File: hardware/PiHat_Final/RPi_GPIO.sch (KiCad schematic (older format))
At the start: 1 part, among them J2 RPi_GPIO

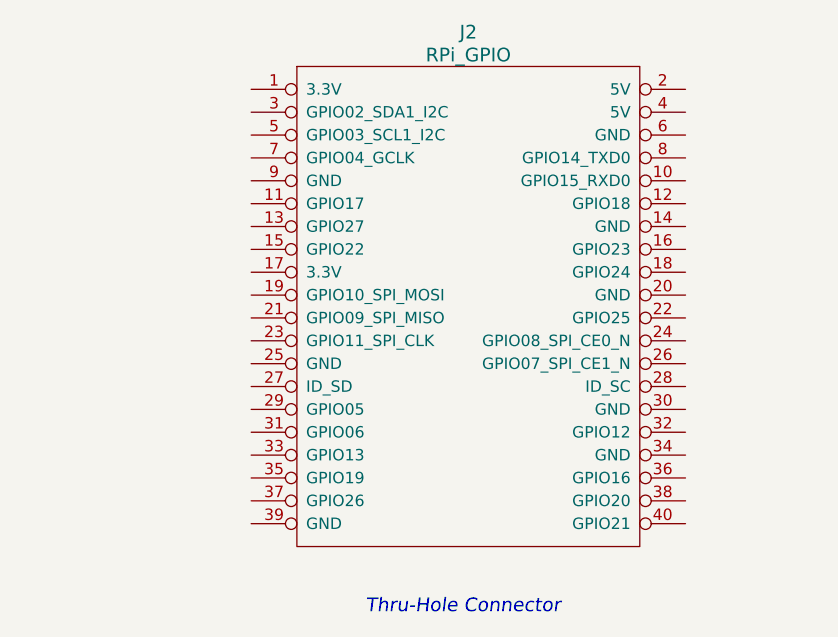
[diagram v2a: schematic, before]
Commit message: Transciever wiring & Power Distribution Changes, modified footprint for Edge SMA, swapped TX/RX on ANTSEL
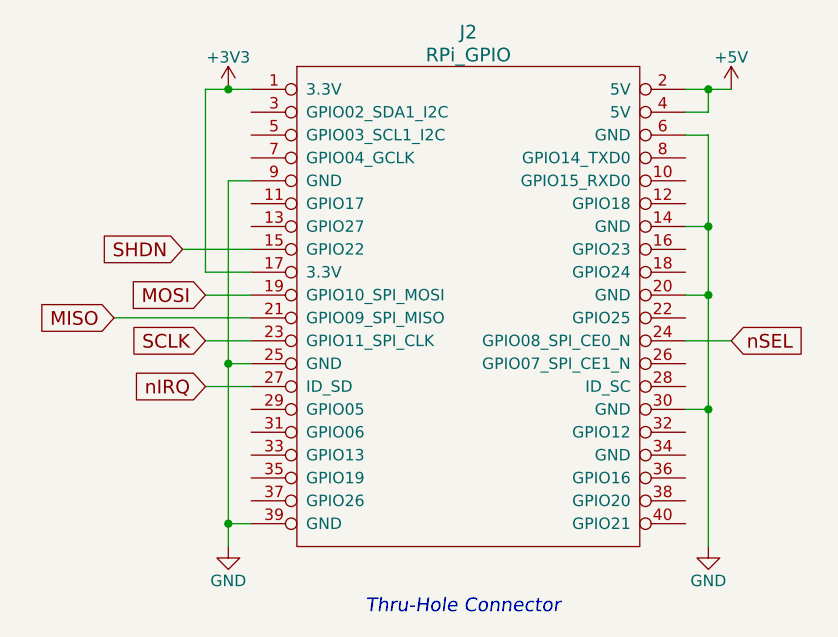
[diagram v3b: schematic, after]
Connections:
- net +3V3: now reaches J2.1 (3.3V)
- net +3V3: now also J2.17 (3.3V)
- net GND: now reaches J2.14 (GND)
- net GND: now also J2.20 (GND), J2.25 (GND), J2.30 (GND), J2.39 (GND), J2.6 (GND), J2.9 (GND)
- net SHDN: now reaches J2.15 (GPIO22)
- net MOSI: now reaches J2.19 (GPIO10_SPI_MOSI)
- net +5V: now reaches J2.2 (5V)
- net +5V: now also J2.4 (5V)
- net MISO: now reaches J2.21 (GPIO09_SPI_MISO)
- net SCLK: now reaches J2.23 (GPIO11_SPI_CLK)
- net nSEL: now reaches J2.24 (GPIO08_SPI_CE0_N)
- net nIRQ: now reaches J2.27 (ID_SD)
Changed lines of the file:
@@
 Text Notes 7800 5000 0    60   Italic 0
 Thru-Hole Connector
+Wire Wire Line
+	9200 2800 9300 2800
+Wire Wire Line
+	9300 2800 9300 2700
+Wire Wire Line
+	9200 2700 9400 2700
+Connection ~ 9300 2700
+Wire Wire Line
+	7100 2700 7300 2700
+$Comp
+L +5V #PWR01
+U 1 1 58FBDD1D
+P 9400 2700
+F 0 "#PWR01" H 9400 2550 50  0001 C CNN
+F 1 "+5V" H 9400 2840 50  0000 C CNN
+F 2 "" H 9400 2700 50  0001 C CNN
+F 3 "" H 9400 2700 50  0001 C CNN
+	1    9400 2700
+	1    0    0    -1
+$EndComp
+$Comp
+L +3V3 #PWR02
+U 1 1 58FBDD33
+P 7200 2700
+F 0 "#PWR02" H 7200 2550 50  0001 C CNN
+F 1 "+3V3" H 7200 2840 50  0000 C CNN
+F 2 "" H 7200 2700 50  0001 C CNN
+F 3 "" H 7200 2700 50  0001 C CNN
+	1    7200 2700
+	1    0    0    -1
+$EndComp
+Wire Wire Line
+	7300 3900 7200 3900
+Wire Wire Line
+	7200 3100 7200 4700
+Wire Wire Line
+	7300 4600 7200 4600
+Connection ~ 7200 4600
+$Comp
+L GND #PWR03
+U 1 1 58FBDD61
+P 7200 4700
+F 0 "#PWR03" H 7200 4450 50  0001 C CNN
+F 1 "GND" H 7200 4550 50  0000 C CNN
+F 2 "" H 7200 4700 50  0001 C CNN
+F 3 "" H 7200 4700 50  0001 C CNN
+	1    7200 4700
+	1    0    0    -1
+$EndComp
+Wire Wire Line
+	9200 3600 9300 3600
+Wire Wire Line
+	9300 2900 9300 4700
+Wire Wire Line
+	9200 4100 9300 4100
+Connection ~ 9300 4100
+Wire Wire Line
+	9300 2900 9200 2900
+Connection ~ 9300 3600
+Wire Wire Line
+	9300 3300 9200 3300
+Connection ~ 9300 3300
+Wire Wire Line
+	7200 3100 7300 3100
+Connection ~ 7200 3900
+$Comp
+L GND #PWR04
+U 1 1 58FBDDDD
+P 9300 4700
+F 0 "#PWR04" H 9300 4450 50  0001 C CNN
+F 1 "GND" H 9300 4550 50  0000 C CNN
+F 2 "" H 9300 4700 50  0001 C CNN
+F 3 "" H 9300 4700 50  0001 C CNN
+	1    9300 4700
+	1    0    0    -1
+$EndComp
+Wire Wire Line
+	7100 2700 7100 3500
+Wire Wire Line
+	7100 3500 7300 3500
+Connection ~ 7200 2700
+Wire Wire Line
+	9200 3800 9400 3800
+Text GLabel 9400 3800 2    60   Input ~ 0
+nSEL
+Wire Wire Line
+	7300 3600 7100 3600
+Wire Wire Line
+	7300 3800 7100 3800
+Text GLabel 7100 3600 0    60   Input ~ 0
+MOSI
+Text GLabel 7100 3800 0    60   Input ~ 0
+SCLK
+Wire Wire Line
+	7300 3700 6700 3700
+Text GLabel 6700 3700 0    60   Input ~ 0
+MISO
+Wire Wire Line
+	7300 4000 7100 4000
+Text GLabel 7100 4000 0    60   Input ~ 0
+nIRQ
+Wire Wire Line
+	7300 3400 7000 3400
+Text GLabel 7000 3400 0    60   Input ~ 0
+SHDN
 $EndSCHEMATC
